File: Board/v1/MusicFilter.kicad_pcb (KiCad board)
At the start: 4 copper layers, 60 x 60 mm, 51 parts, among them J1 TYPE-C-31-M-17, J2 FPC 0.5mm 10P, J3 Conn_01x08_Male, J4 Conn_01x02_Male, P1 SWDPins, SW1 SW_Push, SW2 SW_Push, U1 MP2359, U2 STM32F103CBUx, Y1 8MHz

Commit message: board v2 is out
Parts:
- removed DECO**: Val**, DannyFootprintLibs:FOR_TEST
- removed FB2: 600 @ 100 MHz, Inductor_SMD:L_0603_1608Metric_Pad1.05x0.95mm_HandSolder
- removed J3: Conn_01x08_Male, Connector_PinHeader_2.54mm:PinHeader_1x08_P2.54mm_Vertical
- removed J4: Conn_01x02_Male, Connector_PinHeader_2.54mm:PinHeader_1x02_P2.54mm_Vertical
- removed L1: 47u, Inductor_SMD:L_Abracon_ASPI-0630LR
- added BT1: BK-912, DannyFootprintLibs:BK-912, B.Cu at (97.5, 103.0)
- added C18: 1u, Capacitor_SMD:C_0603_1608Metric_Pad1.08x0.95mm_HandSolder, B.Cu at (101.9, 115.8)
- added C19: 100n, Capacitor_SMD:C_0603_1608Metric_Pad1.08x0.95mm_HandSolder, B.Cu at (98.7, 115.8)
- added C20: 100n, Capacitor_SMD:C_0603_1608Metric_Pad1.08x0.95mm_HandSolder, B.Cu at (95.6, 116.8)
- added D5: WHITE, LED_SMD:LED_0805_2012Metric_Pad1.15x1.40mm_HandSolder, B.Cu at (131.4, 112.4)
- added D6: WHITE, LED_SMD:LED_0805_2012Metric_Pad1.15x1.40mm_HandSolder, B.Cu at (147.0, 112.5)
- added IC1: TP4056X, DannyFootprintLibs:ESOP-8_L4.9-W3.9-P1.27-LS6.0-BL-EP, B.Cu at (75.4, 128.2)
- added R12: 1k5, Resistor_SMD:R_0603_1608Metric_Pad0.98x0.95mm_HandSolder, B.Cu at (135.8, 111.4)
- added R13: 1k5, Resistor_SMD:R_0603_1608Metric_Pad0.98x0.95mm_HandSolder, B.Cu at (151.5, 111.3)
- added Ref**: Val**, DannyFootprintLibs:PIC_Sche2, F.Cu at (97.3, 114.8)
- added SW3: SW_Push, DannyFootprintLibs:SW_Kailh_Choc_V1_HOTSWAP, F.Cu at (131.4, 107.7)
- added SW4: SW_Push, DannyFootprintLibs:SW_Kailh_Choc_V1_HOTSWAP, F.Cu at (147.0, 107.7)
- added SW5: SW_SPDT, Button_Switch_SMD:SW_SPDT_PCM12, B.Cu at (111.0, 137.8)
- C1: value 10n -> 22p
- C10, C13, C14: value 1u -> 100n
- C11: value 10n -> 100n
- C15, C16: value 12p -> 1u
- C17: value 100n -> 1u
- C4: value 10u -> 1u
- C5: value 4u7 -> 100n
- C6, C9: value 100n -> 4u7
- C7: value 100n -> 22p
- D1: value B5819W -> WHITE; footprint Diode_SMD:D_SOD-123 -> LED_SMD:LED_0805_2012Metric_Pad1.15x1.40mm_HandSolder; moved to F.Cu
- D3: value RED -> WHITE; moved to B.Cu
- D4: value BLUE -> WHITE; moved to B.Cu
- F1: value 500mA -> 200mA; footprint Fuse:Fuse_0805_2012Metric_Pad1.15x1.40mm_HandSolder -> Fuse:Fuse_0603_1608Metric_Pad1.05x0.95mm_HandSolder
- H1, H2, H3, H4: value MountingHole_Pad -> MH; footprint MountingHole:MountingHole_4.3mm_M4_Pad_Via -> MountingHole:MountingHole_2.2mm_M2_Pad_Via
- J1: value TYPE-C-31-M-17 -> FPC 0.5mm 10P; footprint DannyFootprintLibs:TYPE-C-SMD_TYPE-C-31-M-16 -> DannyFootprintLibs:96x96 Sharp Memory Lcd With FPC Connector 10p 0.5mm; moved to F.Cu
- J2: value FPC 0.5mm 10P -> TYPE-C-31-M-17; footprint DannyFootprintLibs:FPC 0.5mm 10P -> DannyFootprintLibs:TYPE-C-SMD_TYPE-C-31-M-16
- R10, R11: value 10k -> 1k5
- R2: value 15k -> 1k5
- R3: value 270 -> 17k4
- R5: value 1k5 -> 10k
- R9: value 1k -> 10k
- SW1, SW2: footprint DannyFootprintLibs:SW_Kailh_Choc_V1 -> DannyFootprintLibs:SW_Kailh_Choc_V1_HOTSWAP
- U1: value MP2359 -> STM32F401RCTx; footprint Package_TO_SOT_SMD:SOT-23-6_Handsoldering -> Package_QFP:LQFP-64_10x10mm_P0.5mm
- U2: value STM32F103CBUx -> LP5907MFX-3.3; footprint Package_DFN_QFN:QFN-48-1EP_7x7mm_P0.5mm_EP5.6x5.6mm -> Package_TO_SOT_SMD:SOT-23-5
- Y1: value 8MHz -> 8MHz 20pF; footprint Crystal:Crystal_SMD_3225-4Pin_3.2x2.5mm_HandSoldering -> Crystal:Crystal_SMD_5032-2Pin_5.0x3.2mm_HandSoldering
- moved C1 116.0 mm to (156.0, 136.5), turned to 90 degrees
- moved H3 114.0 mm to (160.0, 130.0)
- moved P1 104.5 mm to (152.7, 93.6), turned to -90 degrees
- moved H2 103.1 mm to (35.0, 130.0)
- moved C7 101.9 mm to (144.0, 136.6)
- moved C5 100.7 mm to (142.6, 132.7), turned to 180 degrees
- moved C13 96.5 mm to (151.5, 127.1), turned to 90 degrees
- moved R1 96.5 mm to (151.5, 123.0)
- moved C4 95.2 mm to (130.0, 130.0)
- moved U1 94.7 mm to (142.5, 124.0), turned to 90 degrees
- moved C9 91.9 mm to (154.5, 127.0)
- moved C11 91.0 mm to (149.6, 130.9), turned to 45 degrees
- moved C8 90.9 mm to (139.1, 133.1), turned to 0 degrees
- moved Y1 89.5 mm to (150.1, 136.5), turned to 180 degrees
- moved C10 89.4 mm to (146.3, 115.8), turned to 180 degrees
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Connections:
- C1 pad 1: BUCK_SW -> OSC_IN
- C1 pad 2: BUCK_BST -> GND
- C10 pad 1: +3.3VA -> +3V3
- C11 pad 1: +3.3VA -> +3V3
- C12 pad 1: DISP -> +3V3
- C13 pad 1: +3.3VA -> +3V3
- C15 pad 1: OSC_IN -> Net-(C15-Pad1)
- C16 pad 1: OSC_OUT -> +3V3
- C17 pad 1: NRST -> +3.3VA
- C2 pad 1: BUCK_EN -> 5V
- C3 pad 2: +3V3 -> BAT
- C4 pad 1: GND -> +3.3VA
- C4 pad 2: +3V3 -> GND
- C5 pad 1: +3V3 -> NRST
- C6 pad 1: +3V3 -> VCAP1
- C7 pad 1: +3V3 -> OSC_OUT
- C8 pad 1: +3V3 -> +3.3VA
- D1 pad 1: BUCK_SW -> CHRG
- D1 pad 2: GND -> Net-(D1-Pad2)
- D2 pad 1: +5V -> 5V
- D3 pad 1: Net-(D3-Pad1) -> KEY1_LED
- D3 pad 2: +3V3 -> Net-(D3-Pad2)
- D4 pad 1: LED_STATUS -> KEY2_LED
- F1 pad 1: Net-(F1-Pad1) -> LDO_IN
- F1 pad 2: Net-(F1-Pad2) -> Net-(C15-Pad1)
- FB1 pad 1: Net-(F1-Pad2) -> +3V3
- FB1 pad 2: BUCK_EN -> +3.3VA
- J1 pad 1: unconnected-(J1-Pad1) -> SPI1_CLK
- J1 pad 2: unconnected-(J1-Pad2) -> SPI1_MOSI
- J1 pad 3: unconnected-(J1-Pad3) -> CS
- J1 pad 4: unconnected-(J1-Pad4) -> EXTCOMM
- J2 pad 1: SPI1_CLK -> unconnected-(J2-Pad1)
- J2 pad 2: SPI1_MOSI -> unconnected-(J2-Pad2)
- J2 pad 3: CS -> unconnected-(J2-Pad3)
- J2 pad 4: EXTCOMM -> unconnected-(J2-Pad4)
- R1 pad 1: BUCK_FB -> BOOT0
- R1 pad 2: +3V3 -> GND
- R10 pad 1: /KEY1 -> Net-(D3-Pad2)
- R10 pad 2: GND -> +3V3
- R11 pad 1: GND -> Net-(D4-Pad2)
- R11 pad 2: /KEY2 -> +3V3
- R2 pad 1: Net-(R2-Pad1) -> Net-(D1-Pad2)
- R2 pad 2: BUCK_FB -> 5V
- R3 pad 2: Net-(R2-Pad1) -> PROG
- R4 pad 1: DISP -> KEY1
- R4 pad 2: +3V3 -> GND
- R5 pad 2: Net-(D3-Pad1) -> KEY2
- R6 pad 1: EXTCOMM -> KEY3
- R7 pad 1: EXTMODE -> GND
- R7 pad 2: GND -> KEY4
- R8 pad 1: BOOT0 -> DISP
- R8 pad 2: GND -> +3V3
- R9 pad 1: Net-(D4-Pad2) -> EXTMODE
- SW1 pad 1: /KEY1 -> KEY1
- SW2 pad 1: /KEY2 -> KEY2
- U1 pad 1: BUCK_BST -> +3V3
- U1 pad 2: GND -> unconnected-(U1-Pad2)
- U1 pad 3: BUCK_FB -> unconnected-(U1-Pad3)
- U1 pad 4: BUCK_EN -> unconnected-(U1-Pad4)
- U1 pad 5: BUCK_EN -> OSC_IN
- U1 pad 6: BUCK_SW -> OSC_OUT
- U2 pad 1: +3V3 -> Net-(C15-Pad1)
- U2 pad 2: unconnected-(U2-Pad2) -> GND
- U2 pad 3: unconnected-(U2-Pad3) -> Net-(C15-Pad1)
- U2 pad 5: OSC_IN -> +3V3
- Y1 pad 2: GND -> OSC_OUT
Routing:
- net +3V3: track 44.8 -> 239.5 mm, vias 18 -> 21
- net KEY1: track 0.00 -> 121.6 mm, vias 0 -> 2
- net KEY2: track 0.00 -> 107.4 mm, vias 0 -> 6
- net KEY1_LED: track 0.00 -> 97.0 mm
- net BAT: track 0.00 -> 89.2 mm, vias 0 -> 7
- net KEY2_LED: track 0.00 -> 81.3 mm
- net /KEY1: track 67.6 -> 0.00 mm, vias 2 -> 0
- net /KEY2: track 54.3 -> 0.00 mm, vias 2 -> 0
- net LED_STATUS: track 49.1 -> 0.00 mm, vias 1 -> 0
- net 5V: track 0.00 -> 36.7 mm
- net KEY3: track 0.00 -> 36.5 mm, vias 0 -> 2
- net CS: track 10.2 -> 44.7 mm
- net DISP: track 14.7 -> 47.9 mm
- net +3.3VA: track 34.4 -> 66.9 mm, vias 4 -> 2
- net +5V: track 32.5 -> 0.00 mm, vias 1 -> 0
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- added copper zone on B.Cu, net GND
- added copper zone on F.Cu, net GND
- removed copper zone on In2.Cu, net +3V3
- removed copper zone on In1.Cu, net GND
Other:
- board size 60 x 60 mm -> 145 x 50 mm
- copper layers 4 -> 2
- board text removed: "DBG"
- board text removed: "JP"
- board text removed: "PWR"

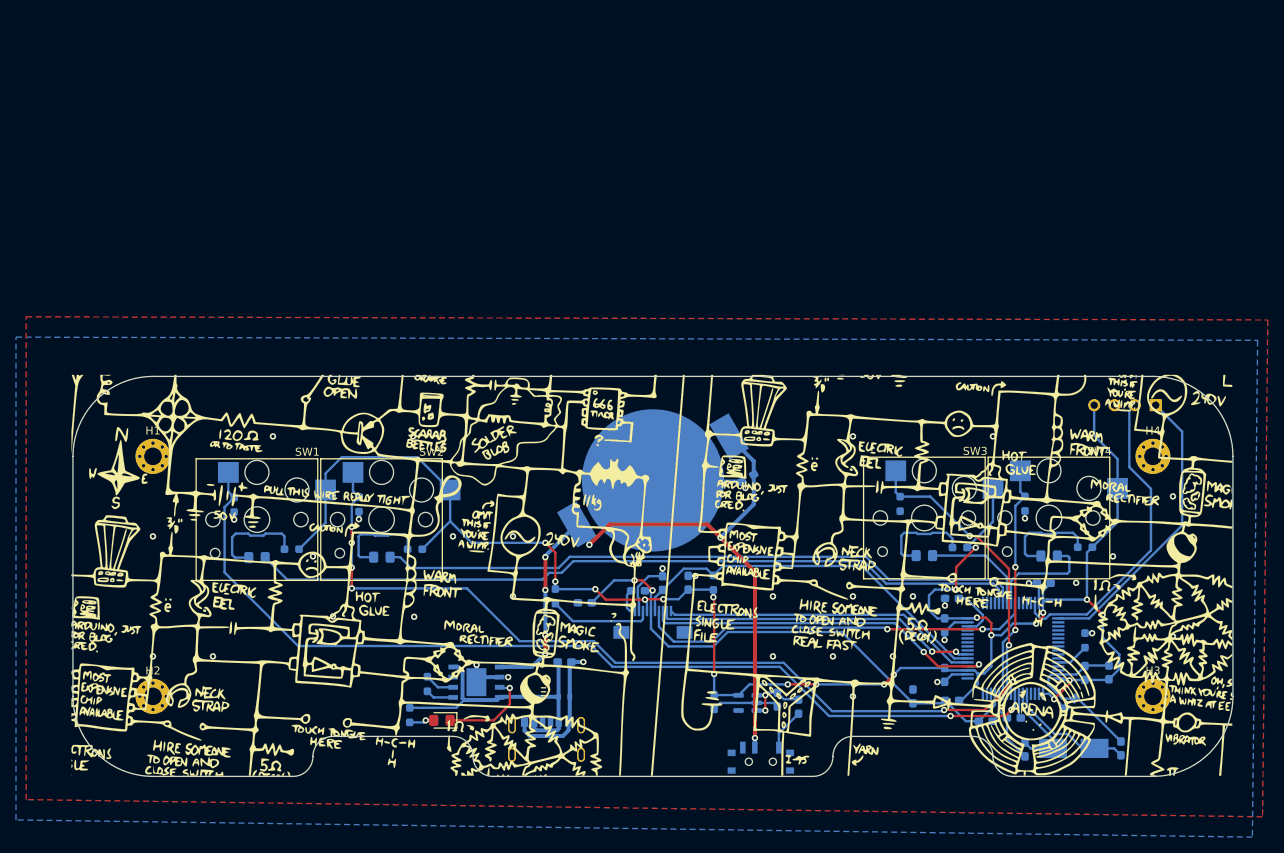
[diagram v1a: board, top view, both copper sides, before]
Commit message: F4 supported
current 20mA to 12mA
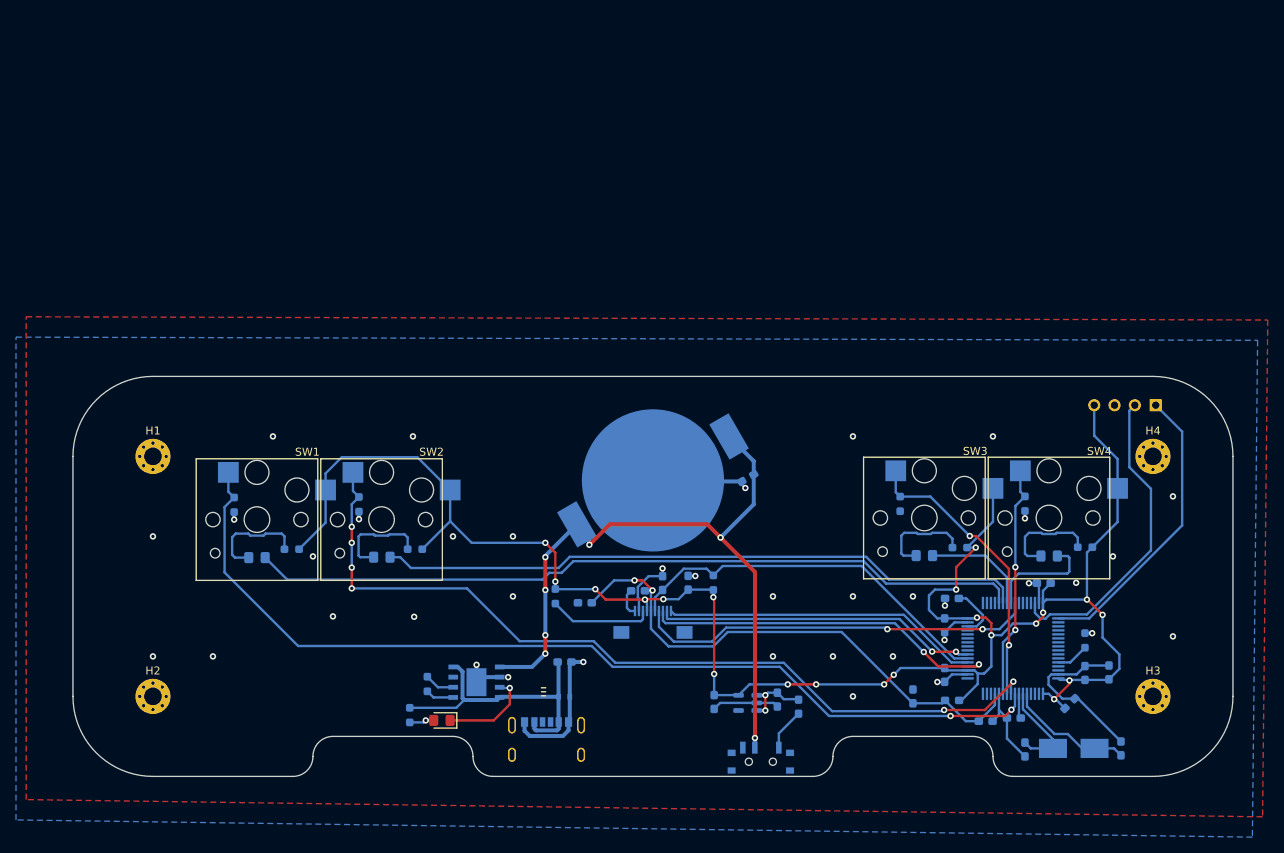
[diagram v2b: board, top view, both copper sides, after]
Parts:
- removed Ref**: Val**, DannyFootprintLibs:PIC_Sche2
